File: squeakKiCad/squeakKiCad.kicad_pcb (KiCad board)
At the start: 4 copper layers, 55.9 x 101.6 mm, 17 parts, among them J1 Conn_01x06_Pin, U1 KB2040, U2 BA00JC5WT, U3 PMW3360DM-T2QU

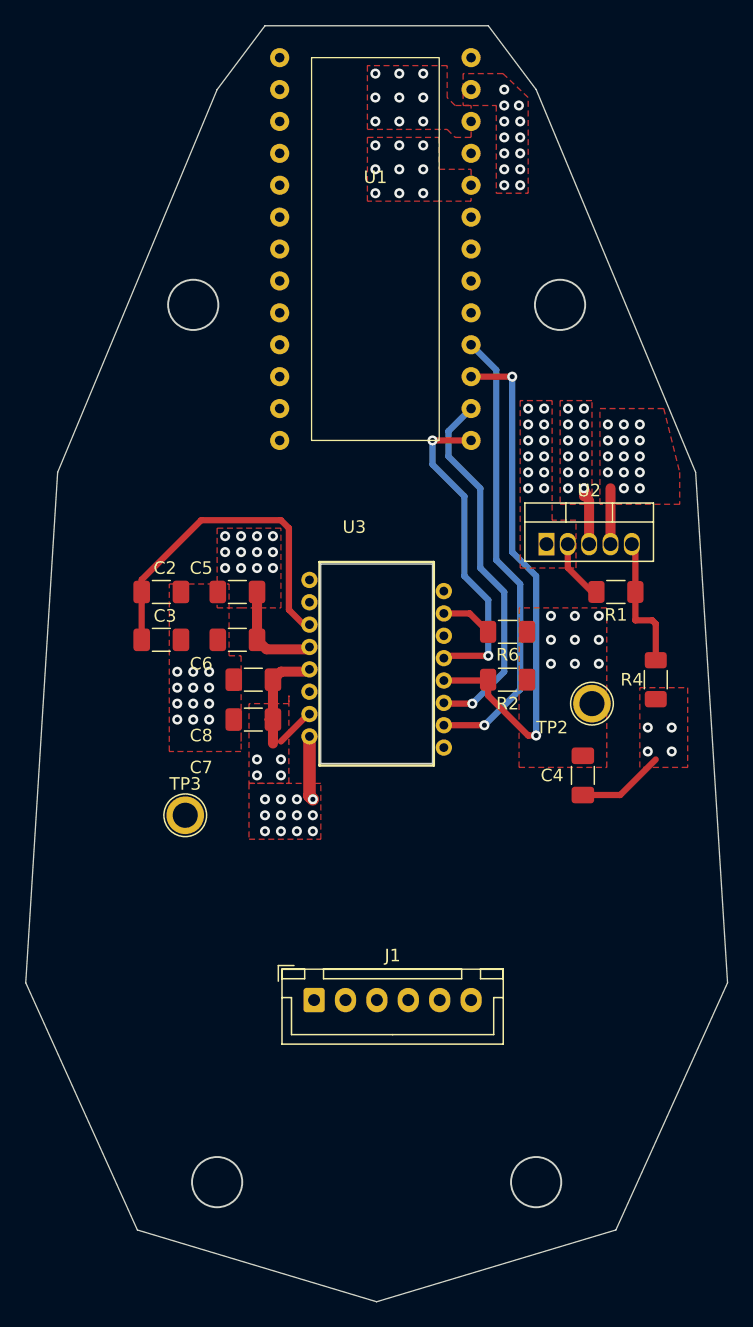
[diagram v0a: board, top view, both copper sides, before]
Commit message: add draft of printable shell
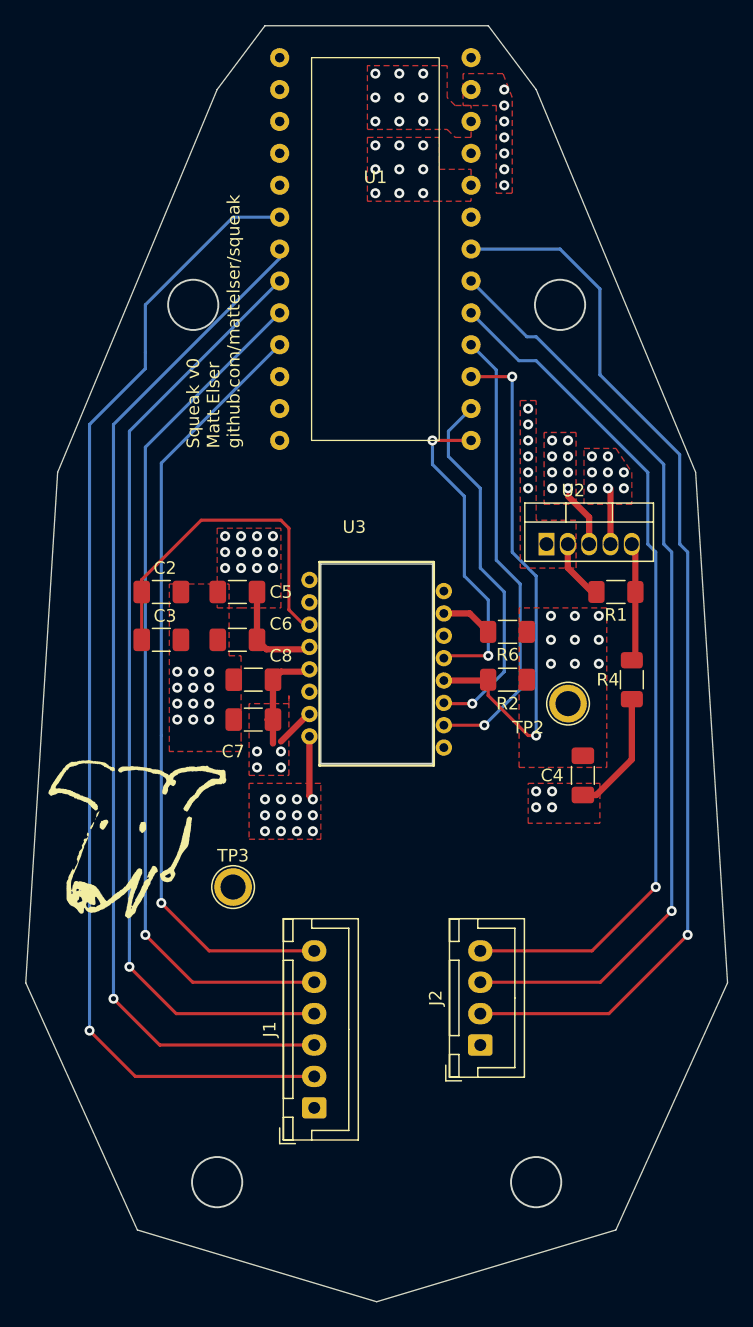
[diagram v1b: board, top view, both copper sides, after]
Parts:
- added G***: LOGO, LOGO, F.Cu at (120.0, 111.6)
- added J2: Conn_01x04_Pin, Connector_JST:JST_XH_B4B-XH-A_1x04_P2.50mm_Vertical, F.Cu at (148.0, 128.8)
- moved J1 8.58 mm to (134.7, 133.8), turned to 90 degrees
- moved TP3 6.87 mm to (128.3, 116.2)
- moved R4 1.91 mm to (160.0, 99.7)
- moved TP2 1.91 mm to (154.9, 101.6)
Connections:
- J1 pad 2: unconnected-(J1-Pin_2-Pad2) -> Net-(J1-Pin_2)
- J1 pad 3: unconnected-(J1-Pin_3-Pad3) -> Net-(J1-Pin_3)
- J1 pad 4: unconnected-(J1-Pin_4-Pad4) -> Net-(J1-Pin_4)
- J1 pad 5: unconnected-(J1-Pin_5-Pad5) -> Net-(J1-Pin_5)
- J1 pad 6: unconnected-(J1-Pin_6-Pad6) -> Net-(J1-Pin_6)
- U1 pad 10: unconnected-(U1-D6-Pad10) -> Net-(J1-Pin_6)
- U1 pad 18: unconnected-(U1-A0-Pad18) -> Net-(J2-Pin_4)
- U1 pad 19: unconnected-(U1-A1-Pad19) -> Net-(J2-Pin_3)
- U1 pad 20: unconnected-(U1-A2-Pad20) -> Net-(J2-Pin_2)
- U1 pad 6: unconnected-(U1-D2-Pad6) -> Net-(J1-Pin_2)
- U1 pad 7: unconnected-(U1-D3-Pad7) -> Net-(J1-Pin_3)
- U1 pad 8: unconnected-(U1-D4-Pad8) -> Net-(J1-Pin_4)
- U1 pad 9: unconnected-(U1-D5-Pad9) -> Net-(J1-Pin_5)
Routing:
- net Net-(J1-Pin_2): track 0.00 -> 92.8 mm, vias 0 -> 1
- net Net-(J2-Pin_2): track 0.00 -> 85.0 mm, vias 0 -> 1
- net Net-(J1-Pin_3): track 0.00 -> 82.9 mm, vias 0 -> 1
- net Net-(J1-Pin_4): track 0.00 -> 75.9 mm, vias 0 -> 1
- net Net-(J2-Pin_3): track 0.00 -> 74.8 mm, vias 0 -> 1
- net Net-(J1-Pin_5): track 0.00 -> 69.0 mm, vias 0 -> 1
- net Net-(J2-Pin_4): track 0.00 -> 68.7 mm, vias 0 -> 1
- net Net-(J1-Pin_6): track 0.00 -> 62.1 mm, vias 0 -> 1
- net GND: track 17.3 -> 19.5 mm, vias 49 -> 45
- net Net-(U2-Adj): track 10.8 -> 9.48 mm
- net 5V: vias 25 -> 13
- net 1.9V: vias 35 -> 29
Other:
- board text added: "Squeak v0 Matt Elser github.com/mattelser/squeak"
